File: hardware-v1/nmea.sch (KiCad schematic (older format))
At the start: 24 parts, among them P1 CONN_01X20, U10 MCP2562, U11 SN65C1168E, U12 INA219

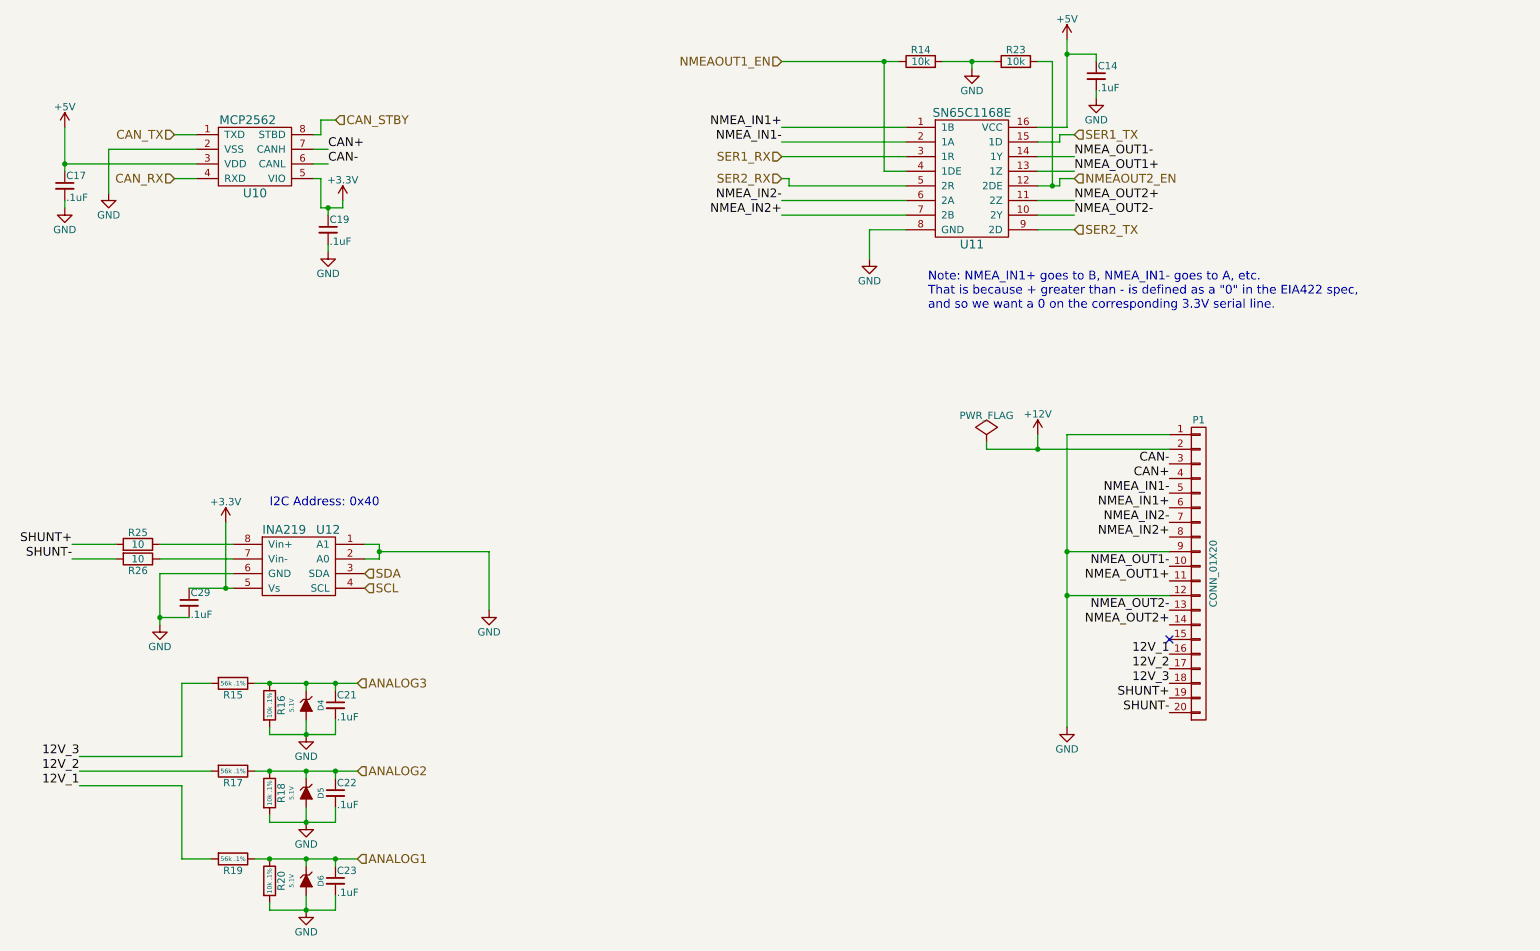
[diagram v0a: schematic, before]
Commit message: Footprint work
 - Fix ina219 footprint (for soic)
 - lm4040
 - sn65c1168e -> tssop16
 - sn74hct245 -> tsso20
 - updated bunch of caps to normal 0603 (not handsolder)
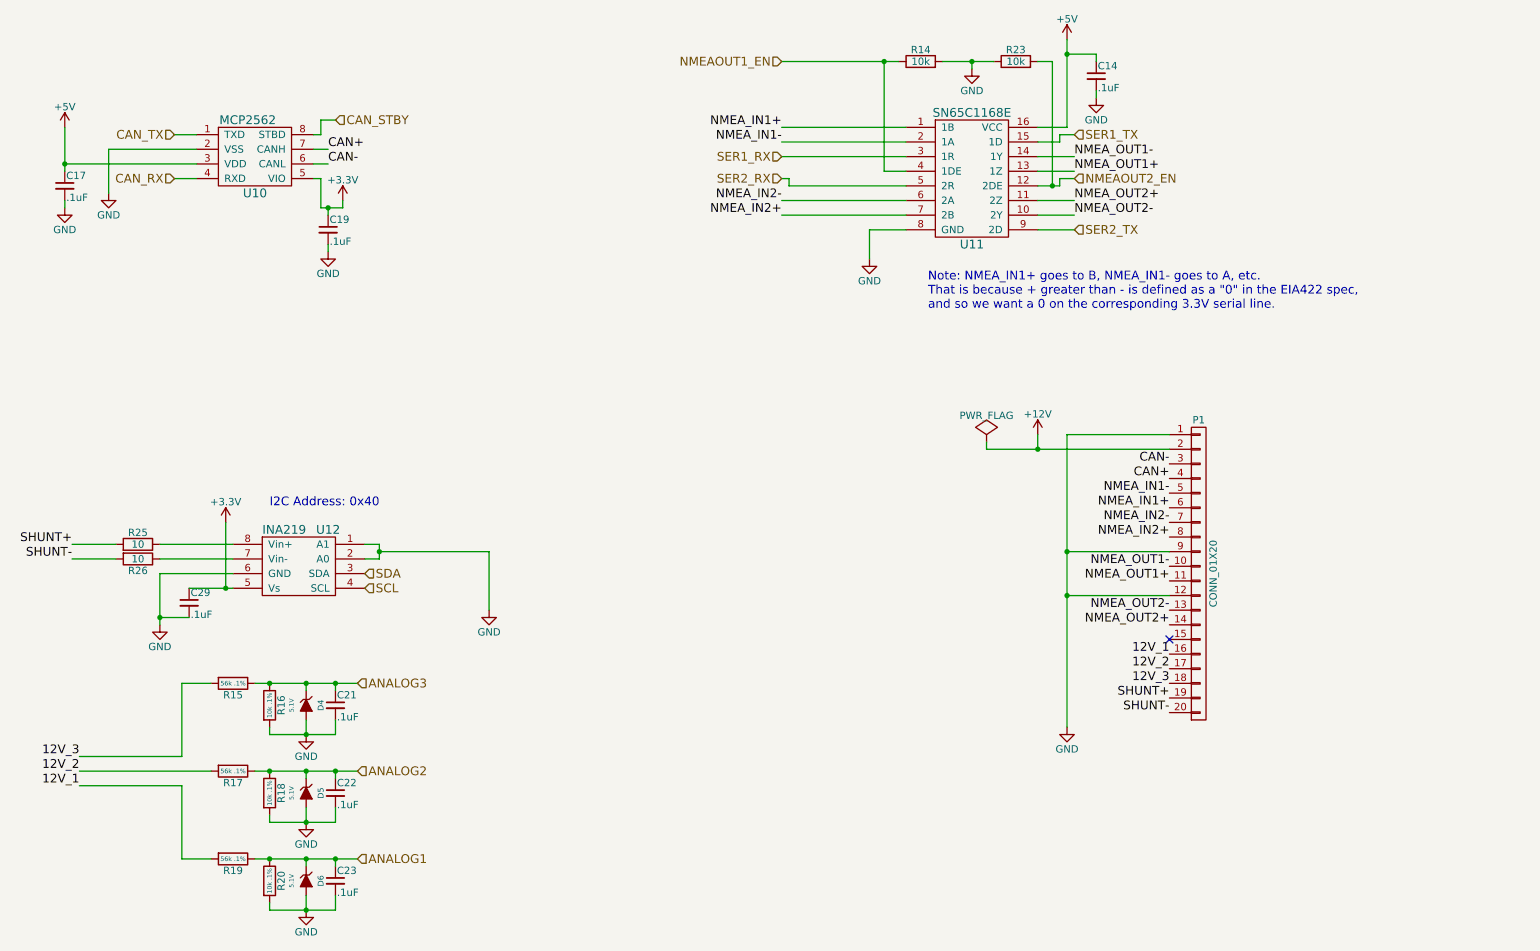
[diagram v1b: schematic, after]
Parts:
- C14, C17, C19, C21, C22, C23, C29: footprint Capacitors_SMD:C_0603_HandSoldering -> Capacitors_SMD:C_0603
- R25, R26: footprint (none) -> Resistors_SMD:R_0603
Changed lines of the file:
@@
 F 0 "C21" H 3460 5720 50  0000 L CNN
 F 1 ".1uF" H 3460 5570 50  0000 L CNN
-F 2 "Capacitors_SMD:C_0603_HandSoldering" H 3450 5650 60  0001 C CNN
+F 2 "Capacitors_SMD:C_0603" H 3450 5650 60  0001 C CNN
 F 3 "" H 3450 5650 60  0000 C CNN
 	1    3450 5650
@@
 $EndComp
 $Comp
-L GND #PWR61
+L GND #PWR049
 U 1 1 5660859F
 P 3250 5850
-F 0 "#PWR61" H 3250 5600 50  0001 C CNN
+F 0 "#PWR049" H 3250 5600 50  0001 C CNN
 F 1 "GND" H 3250 5700 50  0000 C CNN
 F 2 "" H 3250 5850 60  0000 C CNN
@@
 $EndComp
 $Comp
-L +3.3V #PWR52
+L +3.3V #PWR050
 U 1 1 5661817C
 P 3500 2200
-F 0 "#PWR52" H 3500 2050 50  0001 C CNN
+F 0 "#PWR050" H 3500 2050 50  0001 C CNN
 F 1 "+3.3V" H 3500 2340 50  0000 C CNN
 F 2 "" H 3500 2200 60  0000 C CNN
@@
 $EndComp
 $Comp
-L GND #PWR51
+L GND #PWR051
 U 1 1 5661CF45
 P 1900 2150
-F 0 "#PWR51" H 1900 1900 50  0001 C CNN
+F 0 "#PWR051" H 1900 1900 50  0001 C CNN
 F 1 "GND" H 1900 2000 50  0000 C CNN
 F 2 "" H 1900 2150 60  0000 C CNN
@@
 $EndComp
 $Comp
-L +5V #PWR50
+L +5V #PWR052
 U 1 1 5661EB70
 P 1600 1700
-F 0 "#PWR50" H 1600 1550 50  0001 C CNN
+F 0 "#PWR052" H 1600 1550 50  0001 C CNN
 F 1 "+5V" H 1600 1840 50  0000 C CNN
 F 2 "" H 1600 1700 60  0000 C CNN
@@
 F 0 "C19" H 3410 2470 50  0000 L CNN
 F 1 ".1uF" H 3410 2320 50  0000 L CNN
-F 2 "Capacitors_SMD:C_0603_HandSoldering" H 3400 2400 60  0001 C CNN
+F 2 "Capacitors_SMD:C_0603" H 3400 2400 60  0001 C CNN
 F 3 "" H 3400 2400 60  0000 C CNN
 	1    3400 2400
@@
 $EndComp
 $Comp
-L GND #PWR54
+L GND #PWR053
 U 1 1 5663157A
 P 3400 2550
-F 0 "#PWR54" H 3400 2300 50  0001 C CNN
+F 0 "#PWR053" H 3400 2300 50  0001 C CNN
 F 1 "GND" H 3400 2400 50  0000 C CNN
 F 2 "" H 3400 2550 60  0000 C CNN
@@
 F 0 "C17" H 1610 2170 50  0000 L CNN
 F 1 ".1uF" H 1610 2020 50  0000 L CNN
-F 2 "Capacitors_SMD:C_0603_HandSoldering" H 1600 2100 60  0001 C CNN
+F 2 "Capacitors_SMD:C_0603" H 1600 2100 60  0001 C CNN
 F 3 "" H 1600 2100 60  0000 C CNN
 	1    1600 2100
@@
 $EndComp
 $Comp
-L GND #PWR53
+L GND #PWR054
 U 1 1 56633AB1
 P 1600 2250
-F 0 "#PWR53" H 1600 2000 50  0001 C CNN
+F 0 "#PWR054" H 1600 2000 50  0001 C CNN
 F 1 "GND" H 1600 2100 50  0000 C CNN
 F 2 "" H 1600 2250 60  0000 C CNN
@@
 F 0 "C22" H 3460 6320 50  0000 L CNN
 F 1 ".1uF" H 3460 6170 50  0000 L CNN
-F 2 "Capacitors_SMD:C_0603_HandSoldering" H 3450 6250 60  0001 C CNN
+F 2 "Capacitors_SMD:C_0603" H 3450 6250 60  0001 C CNN
 F 3 "" H 3450 6250 60  0000 C CNN
 	1    3450 6250
@@
 $EndComp
 $Comp
-L GND #PWR62
+L GND #PWR055
 U 1 1 5671B320
 P 3250 6450
-F 0 "#PWR62" H 3250 6200 50  0001 C CNN
+F 0 "#PWR055" H 3250 6200 50  0001 C CNN
 F 1 "GND" H 3250 6300 50  0000 C CNN
 F 2 "" H 3250 6450 60  0000 C CNN
@@
 F 0 "C23" H 3460 6920 50  0000 L CNN
 F 1 ".1uF" H 3460 6770 50  0000 L CNN
-F 2 "Capacitors_SMD:C_0603_HandSoldering" H 3450 6850 60  0001 C CNN
+F 2 "Capacitors_SMD:C_0603" H 3450 6850 60  0001 C CNN
 F 3 "" H 3450 6850 60  0000 C CNN
 	1    3450 6850
@@
 $EndComp
 $Comp
-L GND #PWR63
+L GND #PWR056
 U 1 1 5671D29F
 P 3250 7050
-F 0 "#PWR63" H 3250 6800 50  0001 C CNN
+F 0 "#PWR056" H 3250 6800 50  0001 C CNN
 F 1 "GND" H 3250 6900 50  0000 C CNN
 F 2 "" H 3250 7050 60  0000 C CNN
@@
 ANALOG3
 $Comp
-L +12V #PWR56
+L +12V #PWR057
 U 1 1 567F4FFA
 P 8250 3800
-F 0 "#PWR56" H 8250 3650 50  0001 C CNN
+F 0 "#PWR057" H 8250 3650 50  0001 C CNN
 F 1 "+12V" H 8250 3940 50  0000 C CNN
 F 2 "" H 8250 3800 60  0000 C CNN
@@
 $EndComp
 $Comp
-L GND #PWR59
+L GND #PWR058
 U 1 1 56805BCC
 P 2250 5100
-F 0 "#PWR59" H 2250 4850 50  0001 C CNN
+F 0 "#PWR058" H 2250 4850 50  0001 C CNN
 F 1 "GND" H 2250 4950 50  0000 C CNN
 F 2 "" H 2250 5100 60  0000 C CNN
@@
 $EndComp
 $Comp
-L PWR_FLAG #FLG3
+L PWR_FLAG #FLG059
 U 1 1 568074D6
 P 7900 3850
-F 0 "#FLG3" H 7900 3945 50  0001 C CNN
+F 0 "#FLG059" H 7900 3945 50  0001 C CNN
 F 1 "PWR_FLAG" H 7900 4030 50  0000 C CNN
 F 2 "" H 7900 3850 60  0000 C CNN
@@
 $EndComp
 $Comp
-L +3.3V #PWR57
+L +3.3V #PWR060
 U 1 1 56699F39
 P 2700 4400
-F 0 "#PWR57" H 2700 4250 50  0001 C CNN
+F 0 "#PWR060" H 2700 4250 50  0001 C CNN
 F 1 "+3.3V" H 2700 4540 50  0000 C CNN
 F 2 "" H 2700 4400 60  0000 C CNN
@@
 $EndComp
 $Comp
-L GND #PWR58
+L GND #PWR061
 U 1 1 5669B7A7
 P 4500 5000
-F 0 "#PWR58" H 4500 4750 50  0001 C CNN
+F 0 "#PWR061" H 4500 4750 50  0001 C CNN
 F 1 "GND" H 4500 4850 50  0000 C CNN
 F 2 "" H 4500 5000 60  0000 C CNN
@@
 F 0 "C29" H 2460 5020 50  0000 L CNN
 F 1 ".1uF" H 2460 4870 50  0000 L CNN
-F 2 "Capacitors_SMD:C_0603_HandSoldering" H 2450 4950 60  0001 C CNN
+F 2 "Capacitors_SMD:C_0603" H 2450 4950 60  0001 C CNN
 F 3 "" H 2450 4950 60  0000 C CNN
 	1    2450 4950
@@
 $EndComp
 $Comp
-L +5V #PWR47
+L +5V #PWR062
 U 1 1 5665D00E
 P 8450 1100
-F 0 "#PWR47" H 8450 950 50  0001 C CNN
+F 0 "#PWR062" H 8450 950 50  0001 C CNN
 F 1 "+5V" H 8450 1240 50  0000 C CNN
 F 2 "" H 8450 1100 60  0000 C CNN
@@
 F 0 "C14" H 8660 1420 50  0000 L CNN
 F 1 ".1uF" H 8660 1270 50  0000 L CNN
-F 2 "Capacitors_SMD:C_0603_HandSoldering" H 8650 1350 60  0001 C CNN
+F 2 "Capacitors_SMD:C_0603" H 8650 1350 60  0001 C CNN
 F 3 "" H 8650 1350 60  0000 C CNN
 	1    8650 1350
@@
 $EndComp
 $Comp
-L GND #PWR49
+L GND #PWR063
 U 1 1 5665D465
 P 8650 1500
-F 0 "#PWR49" H 8650 1250 50  0001 C CNN
+F 0 "#PWR063" H 8650 1250 50  0001 C CNN
 F 1 "GND" H 8650 1350 50  0000 C CNN
 F 2 "" H 8650 1500 60  0000 C CNN
@@
 $EndComp
 $Comp
-L GND #PWR55
+L GND #PWR064
 U 1 1 566617E0
 P 7100 2600
-F 0 "#PWR55" H 7100 2350 50  0001 C CNN
+F 0 "#PWR064" H 7100 2350 50  0001 C CNN
 F 1 "GND" H 7100 2450 50  0000 C CNN
 F 2 "" H 7100 2600 60  0000 C CNN
@@
 $EndComp
 $Comp
-L GND #PWR48
+L GND #PWR065
 U 1 1 5667B0C5
 P 7800 1300
-F 0 "#PWR48" H 7800 1050 50  0001 C CNN
+F 0 "#PWR065" H 7800 1050 50  0001 C CNN
 F 1 "GND" H 7800 1150 50  0000 C CNN
 F 2 "" H 7800 1300 60  0000 C CNN
@@
 	2400 5500 2600 5500
 Wire Wire Line
-	2900 5500 3000 5500
-Wire Wire Line
-	3000 5500 3250 5500
-Wire Wire Line
-	3250 5500 3450 5500
-Wire Wire Line
-	3450 5500 3600 5500
+	2900 5500 3600 5500
 Connection ~ 3000 5500
 Wire Wire Line
@@
 	3000 5800 3000 5850
 Wire Wire Line
-	3000 5850 3250 5850
-Wire Wire Line
-	3250 5850 3450 5850
+	3000 5850 3450 5850
 Connection ~ 3250 5850
 Wire Wire Line
@@
 	2500 1950 1600 1950
 Wire Wire Line
-	1600 1700 1600 1950
-Wire Wire Line
-	1600 1950 1600 2000
+	1600 1700 1600 2000
 Wire Wire Line
 	3350 1750 3300 1750
 Wire Wire Line
-	3350 2250 3400 2250
-Wire Wire Line
-	3400 2250 3500 2250
+	3350 2250 3500 2250
 Wire Wire Line
 	3400 2300 3400 2250
@@
 	1700 6100 2600 6100
 Wire Wire Line
-	2900 6100 3000 6100
-Wire Wire Line
-	3000 6100 3250 6100
-Wire Wire Line
-	3250 6100 3450 6100
-Wire Wire Line
-	3450 6100 3600 6100
+	2900 6100 3600 6100
 Connection ~ 3000 6100
 Wire Wire Line
@@
 	3000 6400 3000 6450
 Wire Wire Line
-	3000 6450 3250 6450
-Wire Wire Line
-	3250 6450 3450 6450
+	3000 6450 3450 6450
 Connection ~ 3250 6450
 Wire Wire Line
 	2400 6700 2600 6700
 Wire Wire Line
-	2900 6700 3000 6700
-Wire Wire Line
-	3000 6700 3250 6700
-Wire Wire Line
-	3250 6700 3450 6700
-Wire Wire Line
-	3450 6700 3600 6700
+	2900 6700 3600 6700
 Connection ~ 3000 6700
 Wire Wire Line
@@
 	3000 7000 3000 7050
 Wire Wire Line
-	3000 7050 3250 7050
-Wire Wire Line
-	3250 7050 3450 7050
+	3000 7050 3450 7050
 Connection ~ 3250 7050
 Wire Wire Line
@@
 	2750 4750 2250 4750
 Wire Wire Line
-	2250 4750 2250 5050
-Wire Wire Line
-	2250 5050 2250 5100
-Wire Wire Line
-	2450 4850 2700 4850
-Wire Wire Line
-	2700 4850 2750 4850
+	2250 4750 2250 5100
+Wire Wire Line
+	2450 4850 2750 4850
 Wire Wire Line
 	2700 4850 2700 4400
@@
 	3650 4550 3750 4550
 Wire Wire Line
-	3750 4550 3750 4600
-Wire Wire Line
-	3750 4600 3750 4650
+	3750 4550 3750 4650
 Wire Wire Line
 	3750 4650 3650 4650
@@
 	8450 1700 8250 1700
 Wire Wire Line
-	8450 1100 8450 1200
-Wire Wire Line
-	8450 1200 8450 1700
+	8450 1100 8450 1700
 Wire Wire Line
 	8450 1200 8650 1200
@@
 	7100 2400 7100 2600
 Wire Wire Line
-	8250 2100 8350 2100
-Wire Wire Line
-	8350 2100 8400 2100
+	8250 2100 8400 2100
 Wire Wire Line
 	6500 2200 7350 2200
@@
 	6500 1700 7350 1700
 Wire Wire Line
-	7350 1900 7300 1900
-Wire Wire Line
-	7300 1900 7300 1900
-Wire Wire Line
-	7300 1900 6500 1900
-Wire Wire Line
-	6500 1250 7200 1250
-Wire Wire Line
-	7200 1250 7300 1250
+	6500 1900 7350 1900
+Wire Wire Line
+	6500 1250 7300 1250
 Wire Wire Line
 	7200 1250 7200 2000
@@
 Connection ~ 7200 1250
 Wire Wire Line
-	7600 1250 7800 1250
-Wire Wire Line
-	7800 1250 7950 1250
+	7600 1250 7950 1250
 Wire Wire Line
 	7800 1250 7800 1300
@@
 	8400 2050 8400 2100
 Wire Wire Line
-	7900 3900 8250 3900
-Wire Wire Line
-	8250 3900 9150 3900
+	7900 3900 9150 3900
 Wire Wire Line
 	8250 3900 8250 3800
@@
 	8450 4900 9150 4900
 Wire Wire Line
-	8450 3800 8450 4600
-Wire Wire Line
-	8450 4600 8450 4900
-Wire Wire Line
-	8450 4900 8450 5800
+	8450 3800 8450 5800
 Connection ~ 8450 4600
 Connection ~ 8450 4900
 $Comp
-L GND #PWR60
+L GND #PWR066
 U 1 1 566C9EC9
 P 8450 5800
-F 0 "#PWR60" H 8450 5550 50  0001 C CNN
+F 0 "#PWR066" H 8450 5550 50  0001 C CNN
 F 1 "GND" H 8450 5650 50  0000 C CNN
 F 2 "" H 8450 5800 60  0000 C CNN
@@
 F 0 "R25" V 2180 4550 50  0000 C CNN
 F 1 "10" V 2100 4550 50  0000 C CNN
-F 2 "" V 2030 4550 50  0000 C CNN
+F 2 "Resistors_SMD:R_0603" V 2030 4550 50  0001 C CNN
 F 3 "" H 2100 4550 50  0000 C CNN
 	1    2100 4550
@@
 F 0 "R26" V 2180 4650 50  0000 C CNN
 F 1 "10" V 2100 4650 50  0000 C CNN
-F 2 "" V 2030 4650 50  0000 C CNN
+F 2 "Resistors_SMD:R_0603" V 2030 4650 50  0001 C CNN
 F 3 "" H 2100 4650 50  0000 C CNN
 	1    2100 4650

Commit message: fix tl2575
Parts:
- U11: footprint bb:SOIC-16_5.6x10.5mm_Pitch1.27mm-HandSolder -> Housings_SSOP:TSSOP-16_4.4x5mm_Pitch0.65mm
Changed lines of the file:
@@
 F 0 "U11" H 7800 1800 60  0000 C CNN
 F 1 "SN65C1168E" H 7800 2700 60  0000 C CNN
-F 2 "bb:SOIC-16_5.6x10.5mm_Pitch1.27mm-HandSolder" H 7800 2150 60  0001 C CNN
+F 2 "Housings_SSOP:TSSOP-16_4.4x5mm_Pitch0.65mm" H 7800 2150 60  0001 C CNN
 F 3 "" H 7800 2150 60  0000 C CNN
 	1    7800 2150

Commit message: Switch MCP2562 to SOIC8N (not handsolder)
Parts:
- U10: footprint bb:SOIC8N-HandSoldering -> bb:SOIC8N
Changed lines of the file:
@@
 F 0 "U10" H 2900 1550 60  0000 C CNN
 F 1 "MCP2562" H 2850 2050 60  0000 C CNN
-F 2 "bb:SOIC8N-HandSoldering" H 2900 1750 60  0001 C CNN
+F 2 "bb:SOIC8N" H 2900 1750 60  0001 C CNN
 F 3 "" H 2900 1750 60  0000 C CNN
 	1    2900 1850

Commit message: Switch INA219 to SOIC8N (non handsolder)
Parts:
- U12: footprint bb:SOIC8N-HandSoldering -> bb:SOIC8N
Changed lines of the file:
@@
 F 0 "U12" H 3400 4950 60  0000 C CNN
 F 1 "INA219" H 3100 4950 60  0000 C CNN
-F 2 "bb:SOIC8N-HandSoldering" H 3200 4700 60  0001 C CNN
+F 2 "bb:SOIC8N" H 3200 4700 60  0001 C CNN
 F 3 "" H 3200 4700 60  0000 C CNN
 	1    3200 4700
